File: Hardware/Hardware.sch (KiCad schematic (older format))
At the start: 15 parts, among them J1 Conn_01x02, J2 Conn_01x04, J3 Conn_01x03, J4 Conn_01x02, J5 Conn_01x06, J6 Conn_01x08, U1 ESP32-WROOM-32

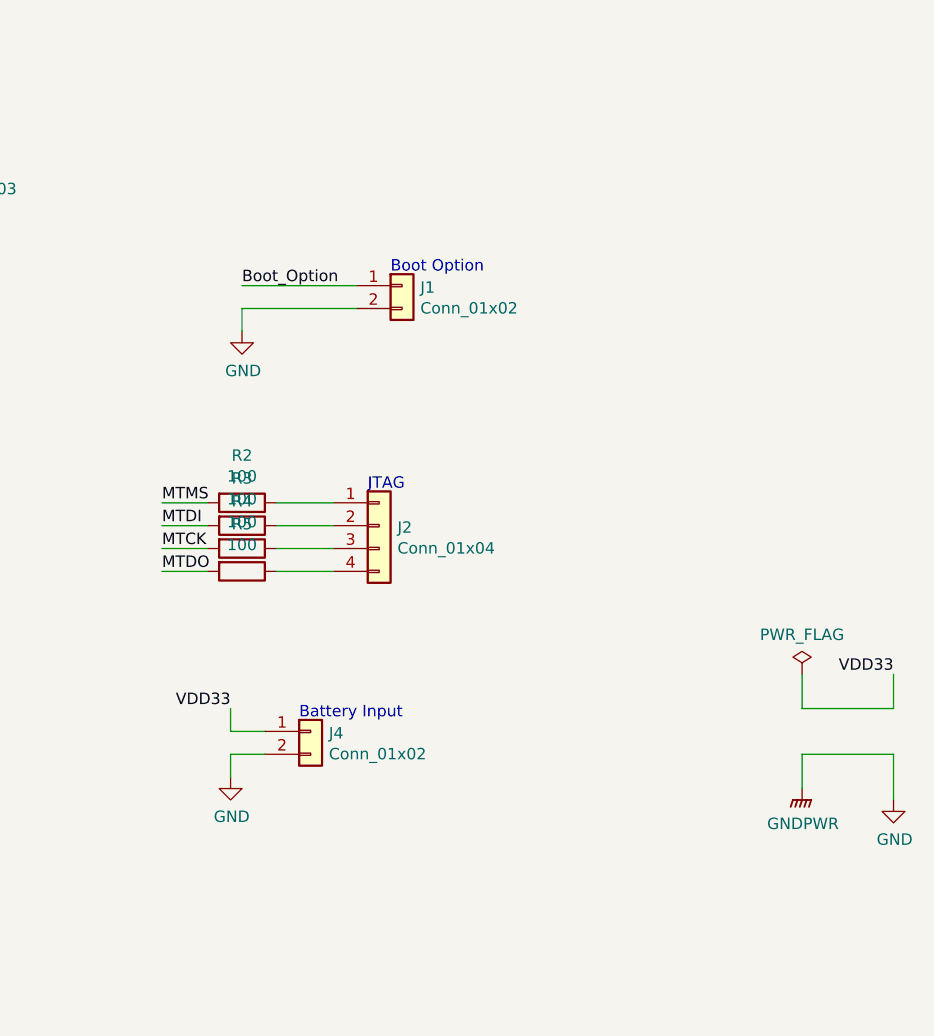
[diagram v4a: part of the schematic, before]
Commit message: Motor port addition and ground plane fix
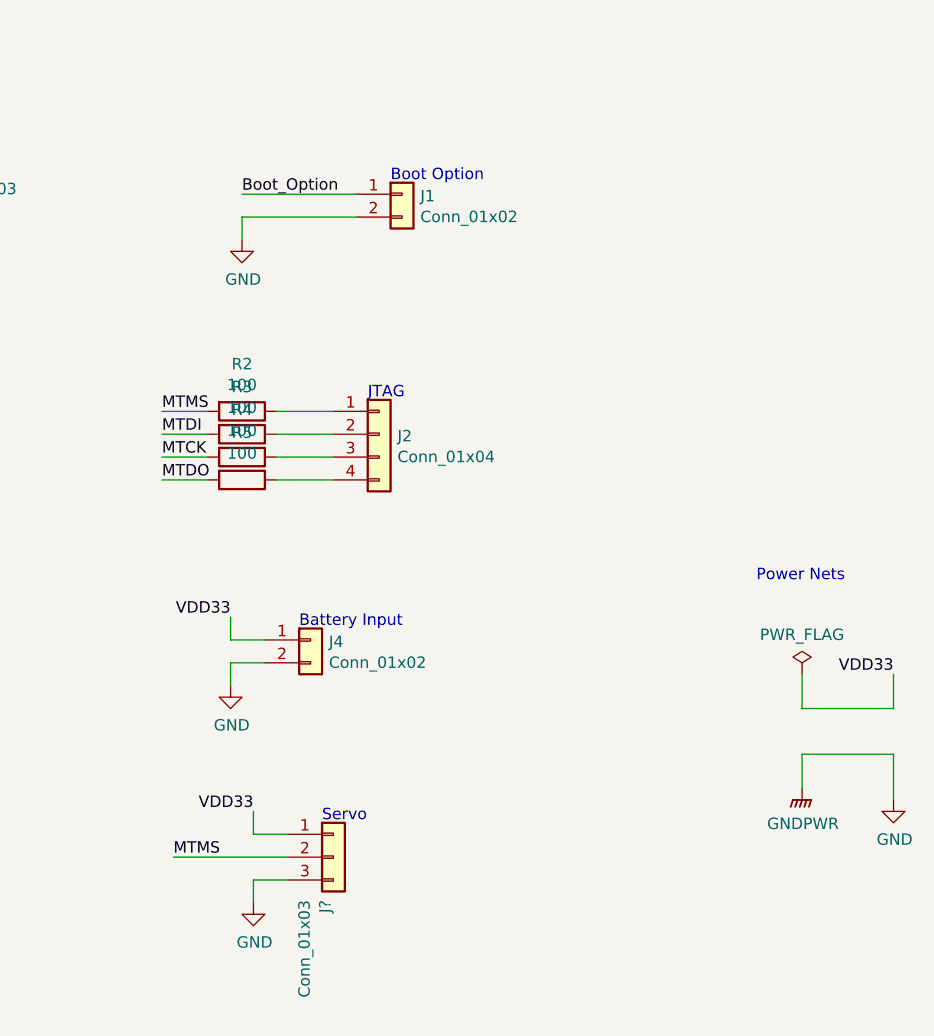
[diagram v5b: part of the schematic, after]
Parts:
- added J?: Conn_01x03, Connector_PinHeader_2.54mm:PinHeader_1x03_P2.54mm_Vertical, symbol Connector_Generic:Conn_01x03
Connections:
- wire segments 56 -> 61
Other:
- note added: "Power Nets"
- note added: "Servo"
- moved on the sheet: J1, J2, J4, R2, R3, R4, R5
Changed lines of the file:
@@
 L Connector_Generic:Conn_01x02 J1
 U 1 1 62092936
-P 6700 2900
-F 0 "J1" H 6780 2892 50  0000 L CNN
-F 1 "Conn_01x02" H 6780 2801 50  0000 L CNN
-F 2 "Connector_PinHeader_2.54mm:PinHeader_1x02_P2.54mm_Vertical" H 6700 2900 50  0001 C CNN
-F 3 "~" H 6700 2900 50  0001 C CNN
-	1    6700 2900
-	1    0    0    -1
-$EndComp
-Text Notes 6650 2850 0    50   ~ 0
+P 6700 2500
+F 0 "J1" H 6780 2492 50  0000 L CNN
+F 1 "Conn_01x02" H 6780 2401 50  0000 L CNN
+F 2 "Connector_PinHeader_2.54mm:PinHeader_1x02_P2.54mm_Vertical" H 6700 2500 50  0001 C CNN
+F 3 "~" H 6700 2500 50  0001 C CNN
+	1    6700 2500
+	1    0    0    -1
+$EndComp
+Text Notes 6650 2450 0    50   ~ 0
 Boot Option\n
 Wire Wire Line
-	6000 2900 6500 2900
+	6000 2500 6500 2500
 $Comp
 L power:GND #PWR0104
 U 1 1 62094E3B
-P 6000 3100
-F 0 "#PWR0104" H 6000 2850 50  0001 C CNN
-F 1 "GND" H 6005 2927 50  0000 C CNN
-F 2 "" H 6000 3100 50  0001 C CNN
-F 3 "" H 6000 3100 50  0001 C CNN
-	1    6000 3100
-	1    0    0    -1
-$EndComp
-Wire Wire Line
-	6000 3000 6000 3100
-Wire Wire Line
-	6000 3000 6500 3000
+P 6000 2700
+F 0 "#PWR0104" H 6000 2450 50  0001 C CNN
+F 1 "GND" H 6005 2527 50  0000 C CNN
+F 2 "" H 6000 2700 50  0001 C CNN
+F 3 "" H 6000 2700 50  0001 C CNN
+	1    6000 2700
+	1    0    0    -1
+$EndComp
+Wire Wire Line
+	6000 2600 6000 2700
+Wire Wire Line
+	6000 2600 6500 2600
 $Comp
 L Connector_Generic:Conn_01x03 J3
@@
 L Connector_Generic:Conn_01x04 J2
 U 1 1 6209B1FA
-P 6600 3950
-F 0 "J2" H 6680 3942 50  0000 L CNN
-F 1 "Conn_01x04" H 6680 3851 50  0000 L CNN
-F 2 "Connector_PinHeader_2.54mm:PinHeader_1x04_P2.54mm_Vertical" H 6600 3950 50  0001 C CNN
-F 3 "~" H 6600 3950 50  0001 C CNN
-	1    6600 3950
-	1    0    0    -1
-$EndComp
-Text Notes 6550 3800 0    50   ~ 0
+P 6600 3550
+F 0 "J2" H 6680 3542 50  0000 L CNN
+F 1 "Conn_01x04" H 6680 3451 50  0000 L CNN
+F 2 "Connector_PinHeader_2.54mm:PinHeader_1x04_P2.54mm_Vertical" H 6600 3550 50  0001 C CNN
+F 3 "~" H 6600 3550 50  0001 C CNN
+	1    6600 3550
+	1    0    0    -1
+$EndComp
+Text Notes 6550 3400 0    50   ~ 0
 JTAG
 Wire Wire Line
-	6400 3850 6150 3850
-Wire Wire Line
-	6400 3950 6150 3950
-Wire Wire Line
-	6400 4150 6150 4150
-Text Label 5650 4050 0    50   ~ 0
+	6400 3450 6150 3450
+Wire Wire Line
+	6400 3550 6150 3550
+Wire Wire Line
+	6400 3750 6150 3750
+Text Label 5650 3650 0    50   ~ 0
 MTCK
-Text Label 5650 4150 0    50   ~ 0
+Text Label 5650 3750 0    50   ~ 0
 MTDO
-Text Label 6000 2900 0    50   ~ 0
+Text Label 6000 2500 0    50   ~ 0
 Boot_Option
 Wire Wire Line
-	6400 4050 6150 4050
+	6400 3650 6150 3650
 $Comp
 L Device:R R2
 U 1 1 6209F2AC
-P 6000 3850
-F 0 "R2" V 5793 3850 50  0000 C CNN
-F 1 "100" V 5884 3850 50  0000 C CNN
-F 2 "Resistor_THT:R_Axial_DIN0204_L3.6mm_D1.6mm_P2.54mm_Vertical" V 5930 3850 50  0001 C CNN
-F 3 "~" H 6000 3850 50  0001 C CNN
-	1    6000 3850
+P 6000 3450
+F 0 "R2" V 5793 3450 50  0000 C CNN
+F 1 "100" V 5884 3450 50  0000 C CNN
+F 2 "Resistor_THT:R_Axial_DIN0204_L3.6mm_D1.6mm_P2.54mm_Vertical" V 5930 3450 50  0001 C CNN
+F 3 "~" H 6000 3450 50  0001 C CNN
+	1    6000 3450
 	0    1    1    0
 $EndComp
@@
 L Device:R R3
 U 1 1 6209FB1B
-P 6000 3950
-F 0 "R3" V 5793 3950 50  0000 C CNN
-F 1 "100" V 5884 3950 50  0000 C CNN
-F 2 "Resistor_THT:R_Axial_DIN0204_L3.6mm_D1.6mm_P2.54mm_Vertical" V 5930 3950 50  0001 C CNN
-F 3 "~" H 6000 3950 50  0001 C CNN
-	1    6000 3950
+P 6000 3550
+F 0 "R3" V 5793 3550 50  0000 C CNN
+F 1 "100" V 5884 3550 50  0000 C CNN
+F 2 "Resistor_THT:R_Axial_DIN0204_L3.6mm_D1.6mm_P2.54mm_Vertical" V 5930 3550 50  0001 C CNN
+F 3 "~" H 6000 3550 50  0001 C CNN
+	1    6000 3550
 	0    1    1    0
 $EndComp
@@
 L Device:R R4
 U 1 1 620A09BA
-P 6000 4050
-F 0 "R4" V 5793 4050 50  0000 C CNN
-F 1 "100" V 5884 4050 50  0000 C CNN
-F 2 "Resistor_THT:R_Axial_DIN0204_L3.6mm_D1.6mm_P2.54mm_Vertical" V 5930 4050 50  0001 C CNN
-F 3 "~" H 6000 4050 50  0001 C CNN
-	1    6000 4050
+P 6000 3650
+F 0 "R4" V 5793 3650 50  0000 C CNN
+F 1 "100" V 5884 3650 50  0000 C CNN
+F 2 "Resistor_THT:R_Axial_DIN0204_L3.6mm_D1.6mm_P2.54mm_Vertical" V 5930 3650 50  0001 C CNN
+F 3 "~" H 6000 3650 50  0001 C CNN
+	1    6000 3650
 	0    1    1    0
 $EndComp
@@
 L Device:R R5
 U 1 1 620A0BC0
-P 6000 4150
-F 0 "R5" V 5793 4150 50  0000 C CNN
-F 1 "100" V 5884 4150 50  0000 C CNN
-F 2 "Resistor_THT:R_Axial_DIN0204_L3.6mm_D1.6mm_P2.54mm_Vertical" V 5930 4150 50  0001 C CNN
-F 3 "~" H 6000 4150 50  0001 C CNN
-	1    6000 4150
+P 6000 3750
+F 0 "R5" V 5793 3750 50  0000 C CNN
+F 1 "100" V 5884 3750 50  0000 C CNN
+F 2 "Resistor_THT:R_Axial_DIN0204_L3.6mm_D1.6mm_P2.54mm_Vertical" V 5930 3750 50  0001 C CNN
+F 3 "~" H 6000 3750 50  0001 C CNN
+	1    6000 3750
 	0    1    1    0
 $EndComp
 Wire Wire Line
-	5850 3850 5650 3850
-Wire Wire Line
-	5850 3950 5650 3950
-Wire Wire Line
-	5850 4050 5650 4050
-Wire Wire Line
-	5850 4150 5650 4150
-Text Label 5650 3850 0    50   ~ 0
+	5850 3450 5650 3450
+Wire Wire Line
+	5850 3550 5650 3550
+Wire Wire Line
+	5850 3650 5650 3650
+Wire Wire Line
+	5850 3750 5650 3750
+Text Label 5650 3450 0    50   ~ 0
 MTMS
-Text Label 5650 3950 0    50   ~ 0
+Text Label 5650 3550 0    50   ~ 0
 MTDI
 Text Label 3250 3300 0    50   ~ 0
@@
 	3200 3400 3450 3400
 Wire Wire Line
-	5950 4850 6100 4850
+	5950 4450 6100 4450
 $Comp
 L Connector_Generic:Conn_01x02 J4
 U 1 1 620B0A16
-P 6300 4850
-F 0 "J4" H 6380 4842 50  0000 L CNN
-F 1 "Conn_01x02" H 6380 4751 50  0000 L CNN
-F 2 "Connector_PinHeader_2.54mm:PinHeader_1x02_P2.54mm_Vertical" H 6300 4850 50  0001 C CNN
-F 3 "~" H 6300 4850 50  0001 C CNN
-	1    6300 4850
+P 6300 4450
+F 0 "J4" H 6380 4442 50  0000 L CNN
+F 1 "Conn_01x02" H 6380 4351 50  0000 L CNN
+F 2 "Connector_PinHeader_2.54mm:PinHeader_1x02_P2.54mm_Vertical" H 6300 4450 50  0001 C CNN
+F 3 "~" H 6300 4450 50  0001 C CNN
+	1    6300 4450
 	1    0    0    -1
 $EndComp
@@
 L power:GND #PWR0106
 U 1 1 620B0F7E
-P 5950 5050
-F 0 "#PWR0106" H 5950 4800 50  0001 C CNN
-F 1 "GND" H 5955 4877 50  0000 C CNN
-F 2 "" H 5950 5050 50  0001 C CNN
-F 3 "" H 5950 5050 50  0001 C CNN
-	1    5950 5050
-	1    0    0    -1
-$EndComp
-Wire Wire Line
-	6100 4950 5950 4950
-Wire Wire Line
-	5950 4950 5950 5050
-Wire Wire Line
-	5950 4750 5950 4850
-Text Label 5950 4750 2    50   ~ 0
+P 5950 4650
+F 0 "#PWR0106" H 5950 4400 50  0001 C CNN
+F 1 "GND" H 5955 4477 50  0000 C CNN
+F 2 "" H 5950 4650 50  0001 C CNN
+F 3 "" H 5950 4650 50  0001 C CNN
+	1    5950 4650
+	1    0    0    -1
+$EndComp
+Wire Wire Line
+	6100 4550 5950 4550
+Wire Wire Line
+	5950 4550 5950 4650
+Wire Wire Line
+	5950 4350 5950 4450
+Text Label 5950 4350 2    50   ~ 0
 VDD33
-Text Notes 6250 4800 0    50   ~ 0
+Text Notes 6250 4400 0    50   ~ 0
 Battery Input
 $Comp
@@
 	1800 1700 2600 1700
 Connection ~ 1800 2000
+Text Label 5700 5400 0    50   ~ 0
+MTMS
+Wire Wire Line
+	5700 5400 6200 5400
+$Comp
+L Connector_Generic:Conn_01x03 J?
+U 1 1 6211C164
+P 6400 5400
+F 0 "J?" V 6364 5212 50  0000 R CNN
+F 1 "Conn_01x03" V 6273 5212 50  0000 R CNN
+F 2 "Connector_PinHeader_2.54mm:PinHeader_1x03_P2.54mm_Vertical" H 6400 5400 50  0001 C CNN
+F 3 "~" H 6400 5400 50  0001 C CNN
+	1    6400 5400
+	1    0    0    -1
+$EndComp
+Wire Wire Line
+	6050 5300 6200 5300
+$Comp
+L power:GND #PWR?
+U 1 1 6211EACD
+P 6050 5600
+F 0 "#PWR?" H 6050 5350 50  0001 C CNN
+F 1 "GND" H 6055 5427 50  0000 C CNN
+F 2 "" H 6050 5600 50  0001 C CNN
+F 3 "" H 6050 5600 50  0001 C CNN
+	1    6050 5600
+	1    0    0    -1
+$EndComp
+Wire Wire Line
+	6200 5500 6050 5500
+Wire Wire Line
+	6050 5500 6050 5600
+Wire Wire Line
+	6050 5200 6050 5300
+Text Label 6050 5200 2    50   ~ 0
+VDD33
+Text Notes 6350 5250 0    50   ~ 0
+Servo
+Text Notes 8250 4200 0    50   ~ 0
+Power Nets
 $EndSCHEMATC

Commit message: SMD conversion
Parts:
- C1, C2, C3: footprint Capacitor_THT:CP_Radial_D4.0mm_P2.00mm -> Capacitor_SMD:C_0805_2012Metric
- R1, R2, R3, R4, R5: footprint Resistor_THT:R_Axial_DIN0204_L3.6mm_D1.6mm_P2.54mm_Vertical -> Resistor_SMD:R_0805_2012Metric
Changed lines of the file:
@@
 F 0 "C3" H 1915 1896 50  0000 L CNN
 F 1 "0.1uF" H 1915 1805 50  0000 L CNN
-F 2 "Capacitor_THT:CP_Radial_D4.0mm_P2.00mm" H 1838 1700 50  0001 C CNN
+F 2 "Capacitor_SMD:C_0805_2012Metric" H 1838 1700 50  0001 C CNN
 F 3 "~" H 1800 1850 50  0001 C CNN
 	1    1800 1850
@@
 F 0 "C2" H 1415 1896 50  0000 L CNN
 F 1 "10uF" H 1415 1805 50  0000 L CNN
-F 2 "Capacitor_THT:CP_Radial_D4.0mm_P2.00mm" H 1338 1700 50  0001 C CNN
+F 2 "Capacitor_SMD:C_0805_2012Metric" H 1338 1700 50  0001 C CNN
 F 3 "~" H 1300 1850 50  0001 C CNN
 	1    1300 1850
@@
 F 0 "R1" H 1170 2296 50  0000 L CNN
 F 1 "10K" H 1170 2205 50  0000 L CNN
-F 2 "Resistor_THT:R_Axial_DIN0204_L3.6mm_D1.6mm_P2.54mm_Vertical" V 1030 2250 50  0001 C CNN
+F 2 "Resistor_SMD:R_0805_2012Metric" V 1030 2250 50  0001 C CNN
 F 3 "~" H 1100 2250 50  0001 C CNN
 	1    1100 2250
@@
 F 0 "C1" H 765 2696 50  0000 L CNN
 F 1 "0.1uF" H 765 2605 50  0000 L CNN
-F 2 "Capacitor_THT:CP_Radial_D4.0mm_P2.00mm" H 688 2500 50  0001 C CNN
+F 2 "Capacitor_SMD:C_0805_2012Metric" H 688 2500 50  0001 C CNN
 F 3 "~" H 650 2650 50  0001 C CNN
 	1    650  2650
@@
 F 0 "R2" V 5793 3450 50  0000 C CNN
 F 1 "100" V 5884 3450 50  0000 C CNN
-F 2 "Resistor_THT:R_Axial_DIN0204_L3.6mm_D1.6mm_P2.54mm_Vertical" V 5930 3450 50  0001 C CNN
+F 2 "Resistor_SMD:R_0805_2012Metric" V 5930 3450 50  0001 C CNN
 F 3 "~" H 6000 3450 50  0001 C CNN
 	1    6000 3450
@@
 F 0 "R3" V 5793 3550 50  0000 C CNN
 F 1 "100" V 5884 3550 50  0000 C CNN
-F 2 "Resistor_THT:R_Axial_DIN0204_L3.6mm_D1.6mm_P2.54mm_Vertical" V 5930 3550 50  0001 C CNN
+F 2 "Resistor_SMD:R_0805_2012Metric" V 5930 3550 50  0001 C CNN
 F 3 "~" H 6000 3550 50  0001 C CNN
 	1    6000 3550
@@
 F 0 "R4" V 5793 3650 50  0000 C CNN
 F 1 "100" V 5884 3650 50  0000 C CNN
-F 2 "Resistor_THT:R_Axial_DIN0204_L3.6mm_D1.6mm_P2.54mm_Vertical" V 5930 3650 50  0001 C CNN
+F 2 "Resistor_SMD:R_0805_2012Metric" V 5930 3650 50  0001 C CNN
 F 3 "~" H 6000 3650 50  0001 C CNN
 	1    6000 3650
@@
 F 0 "R5" V 5793 3750 50  0000 C CNN
 F 1 "100" V 5884 3750 50  0000 C CNN
-F 2 "Resistor_THT:R_Axial_DIN0204_L3.6mm_D1.6mm_P2.54mm_Vertical" V 5930 3750 50  0001 C CNN
+F 2 "Resistor_SMD:R_0805_2012Metric" V 5930 3750 50  0001 C CNN
 F 3 "~" H 6000 3750 50  0001 C CNN
 	1    6000 3750

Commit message: Added mounting holes
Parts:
- added H1, H2: MountingHole, MountingHole:MountingHole_2.1mm, symbol Mechanical:MountingHole
- gave numbers to parts that had none: 1
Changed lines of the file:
@@
 	5700 5400 6200 5400
 $Comp
-L Connector_Generic:Conn_01x03 J?
+L Connector_Generic:Conn_01x03 J7
 U 1 1 6211C164
 P 6400 5400
-F 0 "J?" V 6364 5212 50  0000 R CNN
+F 0 "J7" V 6364 5212 50  0000 R CNN
 F 1 "Conn_01x03" V 6273 5212 50  0000 R CNN
 F 2 "Connector_PinHeader_2.54mm:PinHeader_1x03_P2.54mm_Vertical" H 6400 5400 50  0001 C CNN
@@
 	6050 5300 6200 5300
 $Comp
-L power:GND #PWR?
+L power:GND #PWR0109
 U 1 1 6211EACD
 P 6050 5600
-F 0 "#PWR?" H 6050 5350 50  0001 C CNN
+F 0 "#PWR0109" H 6050 5350 50  0001 C CNN
 F 1 "GND" H 6055 5427 50  0000 C CNN
 F 2 "" H 6050 5600 50  0001 C CNN
@@
 Text Notes 8250 4200 0    50   ~ 0
 Power Nets
+$Comp
+L Mechanical:MountingHole H1
+U 1 1 6257BFE1
+P 8300 1400
+F 0 "H1" H 8400 1446 50  0000 L CNN
+F 1 "MountingHole" H 8400 1355 50  0000 L CNN
+F 2 "MountingHole:MountingHole_2.1mm" H 8300 1400 50  0001 C CNN
+F 3 "~" H 8300 1400 50  0001 C CNN
+	1    8300 1400
+	1    0    0    -1
+$EndComp
+$Comp
+L Mechanical:MountingHole H2
+U 1 1 6257CCB1
+P 8300 1700
+F 0 "H2" H 8400 1746 50  0000 L CNN
+F 1 "MountingHole" H 8400 1655 50  0000 L CNN
+F 2 "MountingHole:MountingHole_2.1mm" H 8300 1700 50  0001 C CNN
+F 3 "~" H 8300 1700 50  0001 C CNN
+	1    8300 1700
+	1    0    0    -1
+$EndComp
 $EndSCHEMATC

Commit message: connector fix
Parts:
- removed J3: Conn_01x03, Connector_PinHeader_2.54mm:PinHeader_1x03_P2.54mm_Vertical, symbol Connector_Generic:Conn_01x03
- added J?: Conn_01x06, symbol Connector_Generic:Conn_01x06
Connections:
- wire segments 61 -> 62
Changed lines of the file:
@@
 Wire Wire Line
 	6000 2600 6500 2600
-$Comp
-L Connector_Generic:Conn_01x03 J3
-U 1 1 62097780
-P 4400 2350
-F 0 "J3" V 4364 2162 50  0000 R CNN
-F 1 "Conn_01x03" V 4273 2162 50  0000 R CNN
-F 2 "Connector_PinHeader_2.54mm:PinHeader_1x03_P2.54mm_Vertical" H 4400 2350 50  0001 C CNN
-F 3 "~" H 4400 2350 50  0001 C CNN
-	1    4400 2350
-	0    -1   -1   0
-$EndComp
 Wire Wire Line
 	3200 2600 4300 2600
@@
 Wire Wire Line
 	4400 2800 3200 2800
-Wire Wire Line
-	4500 2550 4600 2550
-Wire Wire Line
-	4600 2550 4600 2600
-$Comp
-L power:GND #PWR0105
-U 1 1 6209A315
-P 4600 2600
-F 0 "#PWR0105" H 4600 2350 50  0001 C CNN
-F 1 "GND" H 4605 2427 50  0000 C CNN
-F 2 "" H 4600 2600 50  0001 C CNN
-F 3 "" H 4600 2600 50  0001 C CNN
-	1    4600 2600
-	1    0    0    -1
-$EndComp
-Text Notes 4250 2300 0    50   ~ 0
+Text Notes 5200 2050 0    50   ~ 0
 UART Prog
 Text Label 3250 2600 0    50   ~ 0
@@
 	1    0    0    -1
 $EndComp
+$Comp
+L Connector_Generic:Conn_01x06 J?
+U 1 1 625FEE76
+P 5250 2300
+F 0 "J?" H 5330 2292 50  0000 L CNN
+F 1 "Conn_01x06" H 5330 2201 50  0000 L CNN
+F 2 "" H 5250 2300 50  0001 C CNN
+F 3 "~" H 5250 2300 50  0001 C CNN
+	1    5250 2300
+	1    0    0    -1
+$EndComp
+$Comp
+L power:GND #PWR?
+U 1 1 6260035B
+P 3900 2100
+F 0 "#PWR?" H 3900 1850 50  0001 C CNN
+F 1 "GND" H 3905 1927 50  0000 C CNN
+F 2 "" H 3900 2100 50  0001 C CNN
+F 3 "" H 3900 2100 50  0001 C CNN
+	1    3900 2100
+	1    0    0    -1
+$EndComp
+Wire Wire Line
+	3900 2100 3900 1900
+Wire Wire Line
+	3900 1900 5050 1900
+Wire Wire Line
+	5050 1900 5050 2100
 $EndSCHEMATC
